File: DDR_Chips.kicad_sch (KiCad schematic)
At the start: 1 part

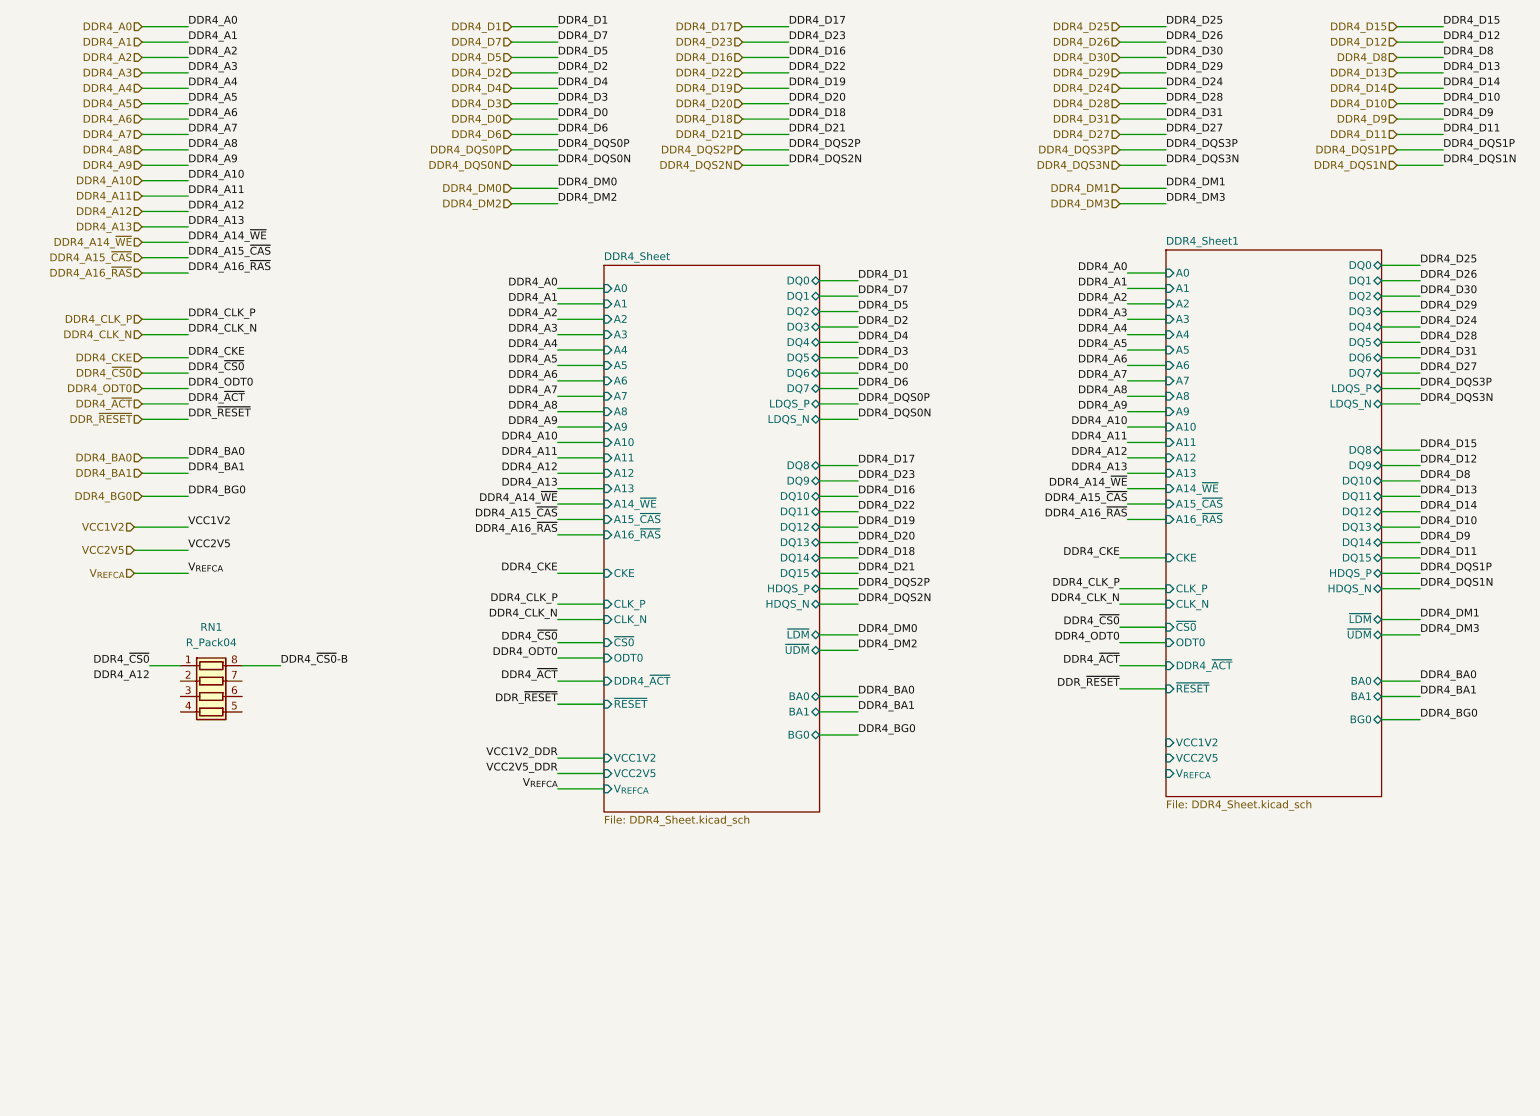
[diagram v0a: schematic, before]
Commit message: connect Resistors of DDR
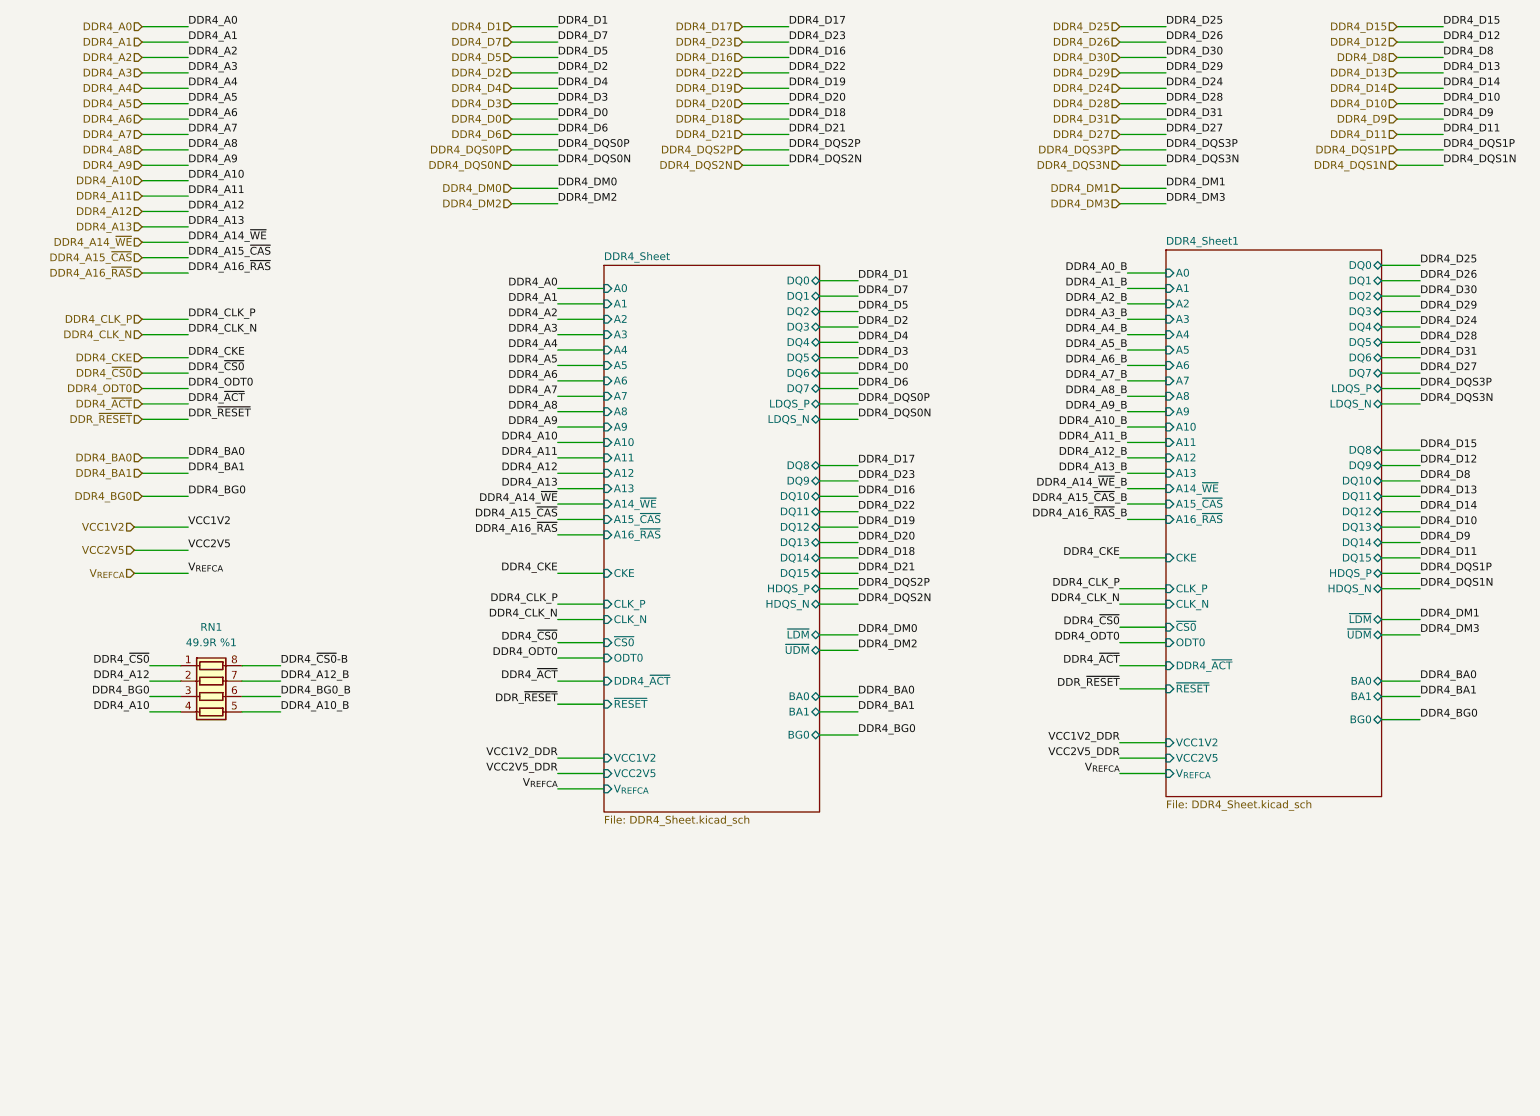
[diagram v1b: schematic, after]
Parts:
- RN1: value R_Pack04 -> 49.9R %1
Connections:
- net DDR4_A10: now also RN1.4 (R4.1)
- net DDR4_A12: now also RN1.2 (R2.1)
- net DDR4_BG0: now also RN1.3 (R3.1)
- net DDR4_A10_B: now reaches RN1.5 (R4.2)
- net DDR4_BG0_B: now reaches RN1.6 (R3.2)
- net DDR4_A12_B: now reaches RN1.7 (R2.2)
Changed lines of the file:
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@@
+    (stroke (width 0) (type default))
+  )
+  (wire (pts (xy 46.99 132.08) (xy 53.34 132.08))
     (stroke (width 0) (type default))
   )
@@
     (stroke (width 0) (type default))
   )
+  (wire (pts (xy 199.39 142.24) (xy 191.77 142.24))
+    (stroke (width 0) (type default))
+  )
   (wire (pts (xy 129.54 24.13) (xy 137.16 24.13))
     (stroke (width 0) (type default))
@@
     (stroke (width 0) (type default))
   )
+  (wire (pts (xy 31.75 127) (xy 36.83 127))
+    (stroke (width 0) (type default))
+  )
   (wire (pts (xy 142.24 73.66) (xy 148.59 73.66))
     (stroke (width 0) (type default))
@@
     (stroke (width 0) (type default))
   )
+  (wire (pts (xy 46.99 129.54) (xy 53.34 129.54))
+    (stroke (width 0) (type default))
+  )
   (wire (pts (xy 106.68 127) (xy 99.06 127))
     (stroke (width 0) (type default))
@@
     (stroke (width 0) (type default))
   )
+  (wire (pts (xy 31.75 132.08) (xy 36.83 132.08))
+    (stroke (width 0) (type default))
+  )
   (wire (pts (xy 191.77 39.37) (xy 199.39 39.37))
     (stroke (width 0) (type default))
@@
     (stroke (width 0) (type default))
   )
+  (wire (pts (xy 199.39 137.16) (xy 191.77 137.16))
+    (stroke (width 0) (type default))
+  )
   (wire (pts (xy 237.49 41.91) (xy 245.11 41.91))
     (stroke (width 0) (type default))
@@
     (stroke (width 0) (type default))
   )
+  (wire (pts (xy 46.99 127) (xy 53.34 127))
+    (stroke (width 0) (type default))
+  )
   (wire (pts (xy 191.77 36.83) (xy 199.39 36.83))
     (stroke (width 0) (type default))
@@
     (stroke (width 0) (type default))
   )
+  (wire (pts (xy 199.39 139.7) (xy 191.77 139.7))
+    (stroke (width 0) (type default))
+  )
   (wire (pts (xy 106.68 90.17) (xy 99.06 90.17))
     (stroke (width 0) (type default))
@@
     (stroke (width 0) (type default))
   )
+  (wire (pts (xy 31.75 129.54) (xy 36.83 129.54))
+    (stroke (width 0) (type default))
+  )
   (wire (pts (xy 142.24 132.08) (xy 148.59 132.08))
     (stroke (width 0) (type default))
@@
     (effects (font (size 1.27 1.27)) (justify left bottom))
   )
-  (label "DDR4_A16_~{RAS}" (at 193.04 100.33 180) (fields_autoplaced)
+  (label "DDR4_A16_~{RAS}_B" (at 193.04 100.33 180) (fields_autoplaced)
     (effects (font (size 1.27 1.27)) (justify right bottom))
   )
@@
     (effects (font (size 1.27 1.27)) (justify left bottom))
   )
+  (label "DDR4_A10_B" (at 53.34 132.08 0) (fields_autoplaced)
+    (effects (font (size 1.27 1.27)) (justify left bottom))
+  )
   (label "DDR4_DQS2N" (at 148.59 114.3 0) (fields_autoplaced)
     (effects (font (size 1.27 1.27)) (justify left bottom))
@@
     (effects (font (size 1.27 1.27)) (justify left bottom))
   )
-  (label "DDR4_A8" (at 193.04 80.01 180) (fields_autoplaced)
+  (label "DDR4_A8_B" (at 193.04 80.01 180) (fields_autoplaced)
     (effects (font (size 1.27 1.27)) (justify right bottom))
   )
@@
     (effects (font (size 1.27 1.27)) (justify left bottom))
   )
-  (label "DDR4_A5" (at 193.04 72.39 180) (fields_autoplaced)
+  (label "DDR4_A5_B" (at 193.04 72.39 180) (fields_autoplaced)
     (effects (font (size 1.27 1.27)) (justify right bottom))
   )
@@
     (effects (font (size 1.27 1.27)) (justify left bottom))
   )
-  (label "DDR4_A15_~{CAS}" (at 193.04 97.79 180) (fields_autoplaced)
+  (label "DDR4_A15_~{CAS}_B" (at 193.04 97.79 180) (fields_autoplaced)
     (effects (font (size 1.27 1.27)) (justify right bottom))
   )
@@
     (effects (font (size 1.27 1.27)) (justify left bottom))
   )
+  (label "V_{REFCA}" (at 191.77 142.24 180) (fields_autoplaced)
+    (effects (font (size 1.27 1.27)) (justify right bottom))
+  )
   (label "DDR4_A5" (at 38.1 31.75 0) (fields_autoplaced)
     (effects (font (size 1.27 1.27)) (justify left bottom))
@@
     (effects (font (size 1.27 1.27)) (justify left bottom))
   )
-  (label "DDR4_A11" (at 193.04 87.63 180) (fields_autoplaced)
+  (label "DDR4_A11_B" (at 193.04 87.63 180) (fields_autoplaced)
     (effects (font (size 1.27 1.27)) (justify right bottom))
   )
@@
     (effects (font (size 1.27 1.27)) (justify left bottom))
   )
-  (label "DDR4_A2" (at 193.04 64.77 180) (fields_autoplaced)
+  (label "DDR4_A2_B" (at 193.04 64.77 180) (fields_autoplaced)
     (effects (font (size 1.27 1.27)) (justify right bottom))
   )
@@
     (effects (font (size 1.27 1.27)) (justify left bottom))
   )
-  (label "DDR4_A0" (at 193.04 59.69 180) (fields_autoplaced)
+  (label "DDR4_A0_B" (at 193.04 59.69 180) (fields_autoplaced)
     (effects (font (size 1.27 1.27)) (justify right bottom))
   )
@@
     (effects (font (size 1.27 1.27)) (justify left bottom))
   )
-  (label "DDR4_A7" (at 193.04 77.47 180) (fields_autoplaced)
+  (label "DDR4_A7_B" (at 193.04 77.47 180) (fields_autoplaced)
     (effects (font (size 1.27 1.27)) (justify right bottom))
   )
@@
     (effects (font (size 1.27 1.27)) (justify left bottom))
   )
-  (label "DDR4_A12" (at 193.04 90.17 180) (fields_autoplaced)
+  (label "DDR4_A12_B" (at 193.04 90.17 180) (fields_autoplaced)
     (effects (font (size 1.27 1.27)) (justify right bottom))
   )
@@
     (effects (font (size 1.27 1.27)) (justify right bottom))
   )
+  (label "DDR4_BG0" (at 31.75 129.54 180) (fields_autoplaced)
+    (effects (font (size 1.27 1.27)) (justify right bottom))
+  )
   (label "DDR4_D23" (at 137.16 21.59 0) (fields_autoplaced)
     (effects (font (size 1.27 1.27)) (justify left bottom))
@@
     (effects (font (size 1.27 1.27)) (justify left bottom))
   )
-  (label "DDR4_A1" (at 193.04 62.23 180) (fields_autoplaced)
+  (label "DDR4_A1_B" (at 193.04 62.23 180) (fields_autoplaced)
     (effects (font (size 1.27 1.27)) (justify right bottom))
   )
@@
     (effects (font (size 1.27 1.27)) (justify right bottom))
   )
-  (label "DDR4_A9" (at 193.04 82.55 180) (fields_autoplaced)
+  (label "DDR4_A9_B" (at 193.04 82.55 180) (fields_autoplaced)
     (effects (font (size 1.27 1.27)) (justify right bottom))
   )
@@
     (effects (font (size 1.27 1.27)) (justify left bottom))
   )
-  (label "DDR4_A4" (at 193.04 69.85 180) (fields_autoplaced)
+  (label "DDR4_BG0_B" (at 53.34 129.54 0) (fields_autoplaced)
+    (effects (font (size 1.27 1.27)) (justify left bottom))
+  )
+  (label "DDR4_A4_B" (at 193.04 69.85 180) (fields_autoplaced)
     (effects (font (size 1.27 1.27)) (justify right bottom))
   )
@@
     (effects (font (size 1.27 1.27)) (justify left bottom))
   )
+  (label "VCC1V2_DDR" (at 191.77 137.16 180) (fields_autoplaced)
+    (effects (font (size 1.27 1.27)) (justify right bottom))
+  )
   (label "DDR4_D2" (at 99.06 26.67 0) (fields_autoplaced)
     (effects (font (size 1.27 1.27)) (justify left bottom))
   )
-  (label "DDR4_A14_~{WE}" (at 193.04 95.25 180) (fields_autoplaced)
+  (label "DDR4_A14_~{WE}_B" (at 193.04 95.25 180) (fields_autoplaced)
     (effects (font (size 1.27 1.27)) (justify right bottom))
   )
@@
     (effects (font (size 1.27 1.27)) (justify left bottom))
   )
-  (label "DDR4_A3" (at 193.04 67.31 180) (fields_autoplaced)
+  (label "DDR4_A3_B" (at 193.04 67.31 180) (fields_autoplaced)
     (effects (font (size 1.27 1.27)) (justify right bottom))
   )
@@
     (effects (font (size 1.27 1.27)) (justify left bottom))
   )
-  (label "DDR4_A10" (at 193.04 85.09 180) (fields_autoplaced)
+  (label "DDR4_A10_B" (at 193.04 85.09 180) (fields_autoplaced)
     (effects (font (size 1.27 1.27)) (justify right bottom))
   )
@@
     (effects (font (size 1.27 1.27)) (justify left bottom))
   )
+  (label "VCC2V5_DDR" (at 191.77 139.7 180) (fields_autoplaced)
+    (effects (font (size 1.27 1.27)) (justify right bottom))
+  )
   (label "DDR4_D31" (at 241.3 73.66 0) (fields_autoplaced)
     (effects (font (size 1.27 1.27)) (justify left bottom))
@@
     (effects (font (size 1.27 1.27)) (justify right bottom))
   )
-  (label "DDR4_A6" (at 193.04 74.93 180) (fields_autoplaced)
+  (label "DDR4_A6_B" (at 193.04 74.93 180) (fields_autoplaced)
     (effects (font (size 1.27 1.27)) (justify right bottom))
   )
@@
     (effects (font (size 1.27 1.27)) (justify right bottom))
   )
-  (label "DDR4_A13" (at 193.04 92.71 180) (fields_autoplaced)
+  (label "DDR4_A13_B" (at 193.04 92.71 180) (fields_autoplaced)
+    (effects (font (size 1.27 1.27)) (justify right bottom))
+  )
+  (label "DDR4_A10" (at 31.75 132.08 180) (fields_autoplaced)
     (effects (font (size 1.27 1.27)) (justify right bottom))
   )
@@
   )
   (label "DDR4_D27" (at 199.39 36.83 0) (fields_autoplaced)
+    (effects (font (size 1.27 1.27)) (justify left bottom))
+  )
+  (label "DDR4_A12_B" (at 53.34 127 0) (fields_autoplaced)
     (effects (font (size 1.27 1.27)) (justify left bottom))
   )
@@
       (effects (font (size 1.27 1.27)))
     )
-    (property "Value" "R_Pack04" (at 41.91 120.65 90)
+    (property "Value" "49.9R %1" (at 41.91 120.65 90)
       (effects (font (size 1.27 1.27)))
     )
@@
       (effects (font (size 1.27 1.27)) hide)
     )
+    (property "LCSC" "" (at 41.91 129.54 0)
+      (effects (font (size 1.27 1.27)) hide)
+    )
+    (property "Description" "" (at 41.91 129.54 0)
+      (effects (font (size 1.27 1.27)) hide)
+    )
+    (property "Vendor" "" (at 41.91 129.54 0)
+      (effects (font (size 1.27 1.27)) hide)
+    )

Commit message: fix naming
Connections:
- net DDR4_~{CS0}-B renamed DDR4_~{CS0}_B
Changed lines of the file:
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@@
     (effects (font (size 1.27 1.27)) (justify left bottom))
   )
-  (label "DDR4_~{CS0}-B" (at 53.34 124.46 0) (fields_autoplaced)
+  (label "DDR4_~{CS0}_B" (at 53.34 124.46 0) (fields_autoplaced)
     (effects (font (size 1.27 1.27)) (justify left bottom))
   )
